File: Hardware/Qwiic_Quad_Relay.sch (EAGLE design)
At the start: 68 parts, among them J2 Qwiic Right Angle, J3 Qwiic Right Angle, J4 AVR_SPI_PROG_3X2TESTPOINTS, J9 POWER_JACK, K1 RELAY-SPDT-JZC-11F, K2 RELAY-SPDT-JZC-11F, K3 RELAY-SPDT-JZC-11F, K4 RELAY-SPDT-JZC-11F, Q1 600mA/40V, Q2 600mA/40V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

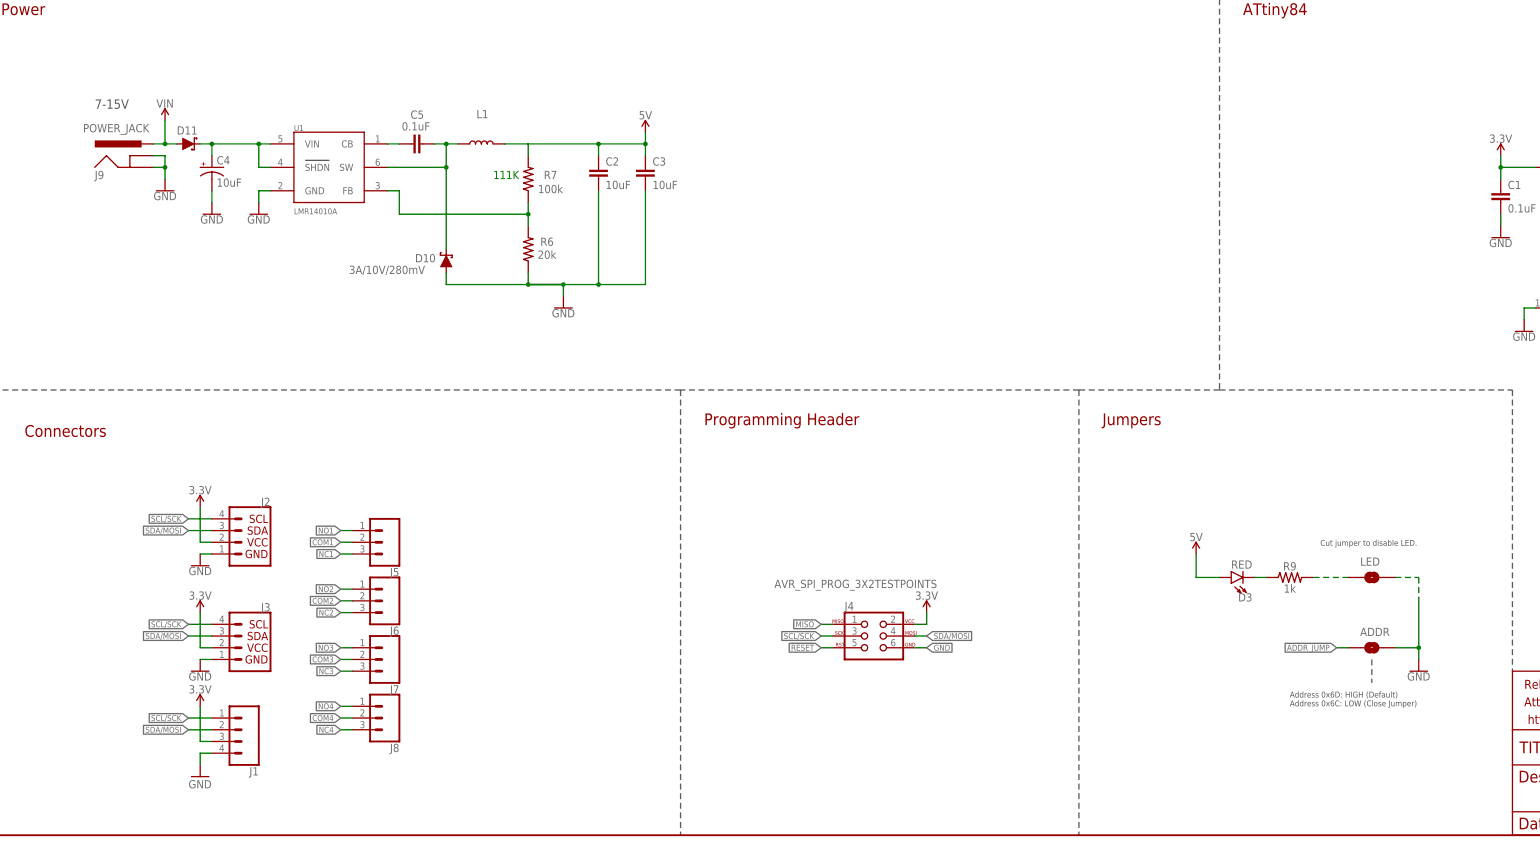
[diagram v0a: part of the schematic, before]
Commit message: Adjusts silk, add bypass jumper, corrects feedback pin resistor values -> output: 5.35V
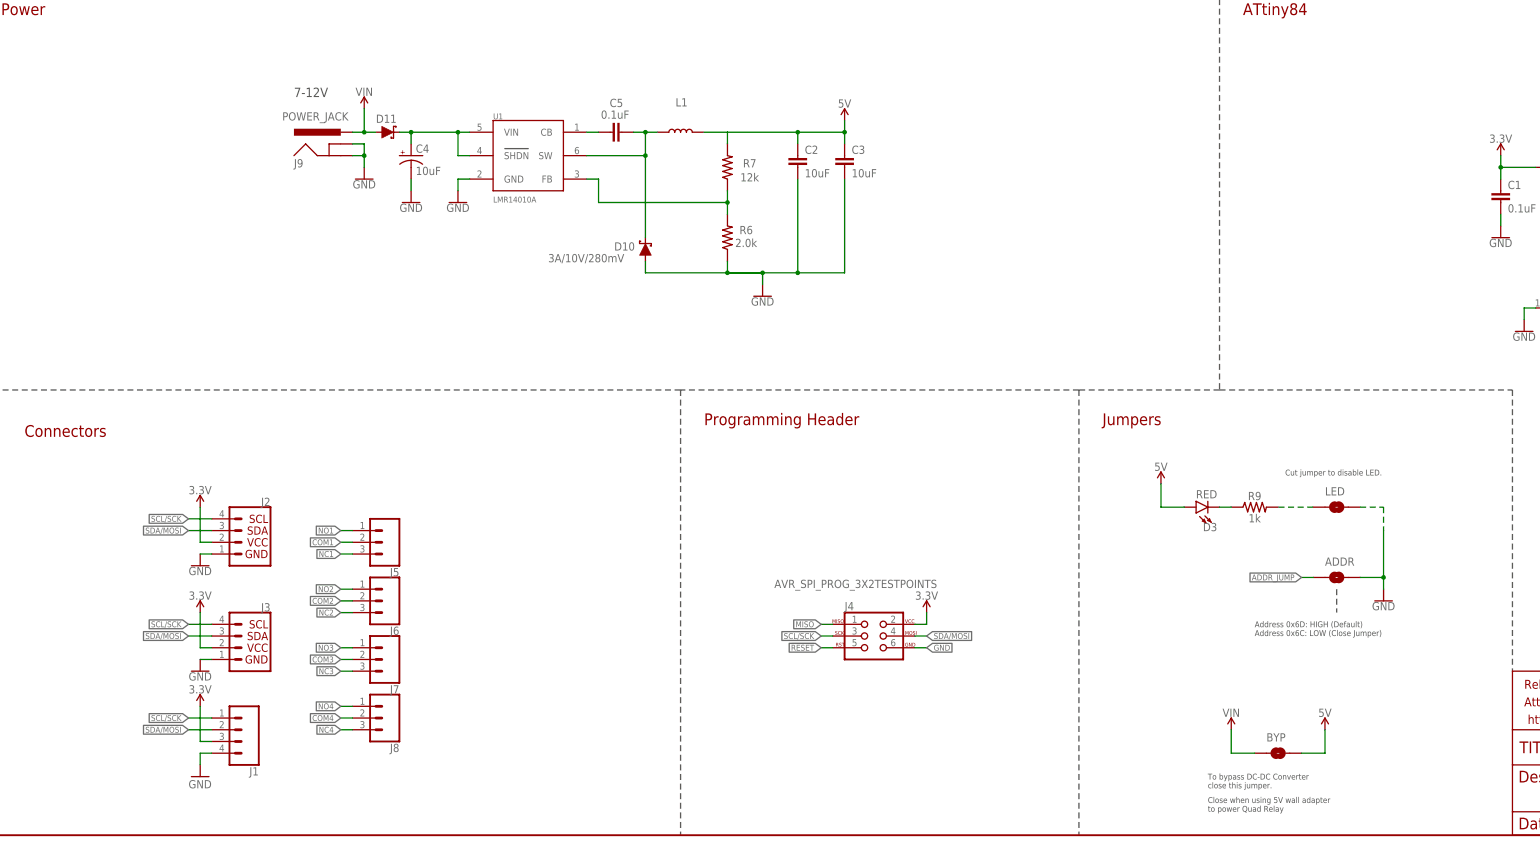
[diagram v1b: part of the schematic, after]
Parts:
- added BYP: JUMPER-SMT_2_NO_SILK, SparkFun-Jumpers:JUMPER-SMT_2_NO_SILK
- R6: value 20k -> 2.0k; device SparkFun-Resistors:20KOHM-0603-1/10W-1% -> SparkFun-Resistors:2.0KOHM-0603-1/10W-5%
- R7: value 100k -> 12k; device SparkFun-Resistors:100KOHM-0603-1/10W-1% -> SparkFun-Resistors:12KOHM-0603-1/10W-1%
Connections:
- net 5V: now also BYP.2
- net VIN: now also BYP.1
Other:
- note added: "7-12V"
- note added: "Close when using 5V wall adapter to power Quad Relay"
- note added: "To bypass DC-DC Converter close this jumper."
- note removed: "111K"
- note removed: "7-15V"
- moved on the sheet: ADDR, C2, C3, C4, C5, D10, D11, D3, J9, L1, LED, R6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

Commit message: Updates schematic
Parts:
- removed ADDR, BYP, LED: JUMPER-SMT_2_NO_SILK, SparkFun-Jumpers:JUMPER-SMT_2_NO_SILK
- added FD1, FD3: FIDUCIAL1X2, SparkFun-Aesthetics:FIDUCIAL1X2
- added JP7: STAND-OFF, SparkFun:STAND-OFF
- C1: value 0.1uF -> 10uF; device SparkFun-Capacitors:0.1UF-0603-25V-(+80/-20%) -> SparkFun-Capacitors:10UF-POLAR-EIA3528-20V-10%(TANT)
- C2: value 10uF -> 0.1uF; device SparkFun-Capacitors:10UF-0603-6.3V-20% -> SparkFun-Capacitors:0.1UF-0402-10V-10%-X7R
- C4: device SparkFun-Capacitors:10UF-POLAR-EIA3528-20V-10%(TANT) -> SparkFun-Capacitors:10UF-0603-6.3V-20%
- C5: device SparkFun-Capacitors:0.1UF-0402-10V-10%-X7R -> SparkFun-Capacitors:0.1UF-0603-25V-(+80/-20%)
- D1, D4: value 1A/23V/620mV -> BLUE; device SparkFun-DiscreteSemi:DIODE-SCHOTTKY-BAT20J -> SparkFun-LED:LED-BLUE0603
- D10: value 3A/10V/280mV -> 1A/23V/620mV; device SparkFun-DiscreteSemi:DIODE-SCHOTTKY-BAT60A -> SparkFun-DiscreteSemi:DIODE-SCHOTTKY-BAT20J
- D11: value 1A/40V/500mV -> RED; device SparkFun-DiscreteSemi:DIODE-SCHOTTKY-SS14 -> SparkFun-LED:LED-RED0603
- D2, D8: value BLUE -> 1A/23V/620mV; device SparkFun-LED:LED-BLUE0603 -> SparkFun-DiscreteSemi:DIODE-SCHOTTKY-BAT20J
- D3: value RED -> 1A/40V/500mV; device SparkFun-LED:LED-RED0603 -> SparkFun-DiscreteSemi:DIODE-SCHOTTKY-SS14
- D6: value 1A/23V/620mV -> 3A/10V/280mV; device SparkFun-DiscreteSemi:DIODE-SCHOTTKY-BAT20J -> SparkFun-DiscreteSemi:DIODE-SCHOTTKY-BAT60A
- J4: value AVR_SPI_PROG_3X2TESTPOINTS -> POWER_JACK; device SparkFun-Connectors:AVR_SPI_PROG_3X2TESTPOINTS -> SparkFun-Connectors:POWER_JACK
- J9: value POWER_JACK -> AVR_SPI_PROG_3X2TESTPOINTS; device SparkFun-Connectors:POWER_JACK -> SparkFun-Connectors:AVR_SPI_PROG_3X2TESTPOINTS
- JP1, JP3: value STAND-OFF -> JUMPER-SMT_2_NO_SILK; device SparkFun:STAND-OFF -> SparkFun-Jumpers:JUMPER-SMT_2_NO_SILK
- JP2: value FIDUCIAL1X2 -> JUMPER-SMT_2_NO_SILK; device SparkFun-Aesthetics:FIDUCIAL1X2 -> SparkFun-Jumpers:JUMPER-SMT_2_NO_SILK
- JP6: value FIDUCIAL1X2 -> STAND-OFF; device SparkFun-Aesthetics:FIDUCIAL1X2 -> SparkFun:STAND-OFF
- LOGO1: value OSHW-LOGOS -> SFE_LOGO_NAME_FLAME.1_INCH; device SparkFun-Aesthetics:OSHW-LOGOS -> SparkFun-Aesthetics:SFE_LOGO_NAME_FLAME.1_INCH
- LOGO2: value SFE_LOGO_NAME_FLAME.1_INCH -> OSHW-LOGOS; device SparkFun-Aesthetics:SFE_LOGO_NAME_FLAME.1_INCH -> SparkFun-Aesthetics:OSHW-LOGOS
- R1: value 33 -> 1k; device SparkFun-Resistors:33OHM-0603-1/10W-1% -> SparkFun-Resistors:1KOHM-0603-1/10W-1%
- R10, R2: value 100 -> 33; device SparkFun-Resistors:100OHM-0603-1/10W-1% -> SparkFun-Resistors:33OHM-0603-1/10W-1%
- R11, R3: value 100 -> 1k; device SparkFun-Resistors:100OHM-0603-1/10W-1% -> SparkFun-Resistors:1KOHM-0603-1/10W-1%
- R12, R13, R14: value 33 -> 100; device SparkFun-Resistors:33OHM-0603-1/10W-1% -> SparkFun-Resistors:100OHM-0603-1/10W-1%
- R15: value 1k -> 100; device SparkFun-Resistors:1KOHM-0603-1/10W-1% -> SparkFun-Resistors:100OHM-0603-1/10W-1%
- R16: value 1k -> 330; device SparkFun-Resistors:1KOHM-0603-1/10W-1% -> SparkFun-Resistors:330OHM-0603-1/10W-1%
- R17: value 1k -> 10k; device SparkFun-Resistors:1KOHM-0603-1/10W-1% -> SparkFun-Resistors:10KOHM-0603-1/10W-1%
- R4: value 1k -> 33; device SparkFun-Resistors:1KOHM-0603-1/10W-1% -> SparkFun-Resistors:33OHM-0603-1/10W-1%
- R5: value 330 -> 12k; device SparkFun-Resistors:330OHM-0603-1/10W-1% -> SparkFun-Resistors:12KOHM-0603-1/10W-1%
- R7: value 12k -> 1k; device SparkFun-Resistors:12KOHM-0603-1/10W-1% -> SparkFun-Resistors:1KOHM-0603-1/10W-1%
- R8: value 10k -> 33; device SparkFun-Resistors:10KOHM-0603-1/10W-1% -> SparkFun-Resistors:33OHM-0603-1/10W-1%
- renumbered FRAME2 to FRAME1, JP8 to FD2, JP9 to FD4, U5 to U4
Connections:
- net !RESET: now also J9.5, R17.2; no longer J4.5, R8.2
- net 3.3V: now also C5.1, J9.2, R17.1; no longer C1.1, J4.2, R8.1
- net 5V: now also C4.1, D10.C, D11.A, D2.C, D8.C, JP1.2, R1.2, R3.2, R9.2; no longer BYP.2, C2.1, D1.C, D3.A, D4.C, D6.C, R15.2, R17.2, R4.2
- net ADDR_JUMP: now also JP3.1; no longer ADDR.1
- net CB: now also C2.1; no longer C5.1
- net FB: now also R5.1; no longer R7.1
- net GND: now also C1.-, C4.2, C5.2, D6.A, J4.GND, J4.GNDBREAK, J9.6, JP2.1, JP3.2; no longer ADDR.2, C1.2, C2.2, C4.-, D10.A, J4.6, J9.GND, J9.GNDBREAK, LED.1
- net MISO: now also J9.1; no longer J4.1
- net N$1: now also D1.A, R1.1; no longer D2.A, R4.1
- net N$10: now also D2.A, R2.2; no longer D1.A, R1.2
- net N$11: now also R13.1; no longer R3.1
- net N$12: now also D4.C, Q2.C, R4.1; no longer D7.C, Q3.C, R12.1
- net N$13: now also D11.C, R11.1; no longer D3.C, R9.1
- net N$14: now also JP2.2, R11.2; no longer LED.2, R9.2
- net N$15: now also D7.C, Q3.C, R8.1; no longer D8.C, Q2.C, R13.1
- net N$17: now also Q4.C, R10.1; no longer Q1.C, R14.1
- net N$18: now also D5.A, R4.2; no longer D6.A, R12.2
- net N$2: now also D1.C, Q1.C, R2.1; no longer D2.C, Q4.C, R1.1
- net N$23: now also D8.A, R8.2; no longer D4.A, R13.2
- net N$24: now also D10.A, R10.2; no longer D5.A, R14.2
- net N$3: now also R15.1; no longer R11.1
- net N$4: now also D4.A, R3.1; no longer D7.A, R15.1
- net N$5: now also R14.1; no longer R10.1
- net N$6: now also R16.1; no longer R5.1
- net N$7: now also D7.A, R7.1; no longer D8.A, R16.1
- net N$8: now also R9.1; no longer R17.1
- net N$9: now also R12.1; no longer R2.1
- net OPTO_1: now also Q1.B; no longer Q4.B
- net OPTO_2: now also Q2.B; no longer Q3.B
- net OPTO_3: now also Q3.B; no longer Q2.B
- net OPTO_4: now also Q4.B; no longer Q1.B
- net RELAY_CTRL1: now also R12.2; no longer R2.2
- net RELAY_CTRL2: now also R13.2; no longer R3.2
- net RELAY_CTRL3: now also R14.2; no longer R10.2
- net RELAY_CTRL4: now also R15.2; no longer R11.2
- net SCL/SCK: now also J9.3; no longer J4.3
- net SDA/MOSI: now also J9.4; no longer J4.4
- net SW: now also C2.2, D6.C; no longer C5.2, D10.C
- net VIN: now also D3.A, J4.PWR, JP1.1; no longer BYP.1, D11.A, J9.PWR
- net VIN_DC_DC: now also C1.+, D3.C; no longer C4.+, D11.C
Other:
- moved on the sheet: C2, C3, C5, D10, D5, D6, D7, J1, J2, J5, J6, J7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

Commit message: Changes standoff to the one used in the SparkFun libraries
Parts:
- JP4, JP5, JP6, JP7: device SparkFun:STAND-OFF -> SparkFun-Hardware:STAND-OFF
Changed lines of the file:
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@@
 <part name="J3" library="SparkFun-Connectors" deviceset="I2C_STANDARD" device="QWIIC" value="Qwiic Right Angle"/>
 <part name="R2" library="SparkFun-Resistors" deviceset="33OHM" device="-0603-1/10W-1%" value="33"/>
-<part name="JP4" library="SparkFun" deviceset="STAND-OFF" device=""/>
-<part name="JP5" library="SparkFun" deviceset="STAND-OFF" device=""/>
+<part name="JP4" library="SparkFun-Hardware" deviceset="STAND-OFF" device=""/>
+<part name="JP5" library="SparkFun-Hardware" deviceset="STAND-OFF" device=""/>
 <part name="FD1" library="SparkFun-Aesthetics" deviceset="FIDUCIAL" device="1X2"/>
 <part name="FD3" library="SparkFun-Aesthetics" deviceset="FIDUCIAL" device="1X2"/>
@@
 <part name="D11" library="SparkFun-LED" deviceset="LED-RED" device="0603" value="RED"/>
 <part name="Q1" library="SparkFun-DiscreteSemi" deviceset="TRANS_NPN" device="-MMBT2222AL" value="600mA/40V"/>
-<part name="JP6" library="SparkFun" deviceset="STAND-OFF" device=""/>
-<part name="JP7" library="SparkFun" deviceset="STAND-OFF" device=""/>
+<part name="JP6" library="SparkFun-Hardware" deviceset="STAND-OFF" device=""/>
+<part name="JP7" library="SparkFun-Hardware" deviceset="STAND-OFF" device=""/>
 <part name="J5" library="SparkFun-Connectors" deviceset="CONN_03" device="-SCREW-5MM"/>
 <part name="FD2" library="SparkFun-Aesthetics" deviceset="FIDUCIAL" device="1X2"/>
